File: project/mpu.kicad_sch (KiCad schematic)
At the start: 0 parts

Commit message: Added CubeMX project and some schematic components are added
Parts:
- added C1, C2: 2u2, bozi:GRM03_T09, symbol Device:C
- added C10, C11: 6p, bozi:GCM15_T05, symbol Device:C
- added C103, C105, C4, C7: 100n, bozi:GRM15_T05, symbol Device:C
- added C104, C3, C5, C6: 1u, bozi:GRM03_T09, symbol Device:C
- added C8, C9: 10p, bozi:GRM15_T05, symbol Device:C
- added R1: 240, bozi:RESC1005X37N_edit, symbol Device:R
- added R2: 0, bozi:RESC1005X37N_edit, symbol Device:R
- added R20, R21, R22: 2K4, bozi:RESC1005X37N_edit, symbol Device:R
- added R23: 3K, bozi:RESC1005X37N_edit, symbol Device:R
- added TP13, TP16, TP17, TP18, TP19: TestPoint, TestPoint:TestPoint_Pad_D1.0mm, symbol Connector:TestPoint
- added U1: ~, symbol bozi:STM32MP135FAF
- added Y1: 24MHz, bozi:ABM11AIG16000MHZ81ZT_edit, symbol Device:Crystal_GND24
- added Y2: Crystal, bozi:ABS07AIG_edit, symbol Device:Crystal
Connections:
- new net: C11.1, R2.1, Y2.1
- new net: R23.1, U1.W12 (USB_RREF)
- new net: C2.2, U1.V14 (VDDA1V1_REG)
- new net: C1.2, U1.W15 (VDDA1V8_REG)
- new net: TP13.1, U1.W3 (PWR_CPU_ON)
- new net: R1.2, U1.R20 (DDR_ZQ)
- new net BOOT0: U1.Y17 (PI4-BOOT0)
- new net BOOT1: U1.AA15 (PI5-BOOT1)
- new net BOOT2: U1.Y15 (PI6-BOOT2)
- new net DDR_A0: U1.H20 (DDR_A0)
- new net DDR_A1: U1.N21 (DDR_A1)
- new net DDR_A10: U1.L18 (DDR_A10)
- new net DDR_A11: U1.N17 (DDR_A11)
- new net DDR_A12: U1.M19 (DDR_A12)
- new net DDR_A13: U1.G19 (DDR_A13)
- new net DDR_A2: U1.G20 (DDR_A2)
- new net DDR_A3: U1.H19 (DDR_A3)
- new net DDR_A4: U1.R19 (DDR_A4)
- new net DDR_A5: U1.F20 (DDR_A5)
- new net DDR_A6: U1.R21 (DDR_A6)
- new net DDR_A7: U1.J17 (DDR_A7)
- new net DDR_A8: U1.P19 (DDR_A8)
- new net DDR_A9: U1.G21 (DDR_A9)
- new net DDR_BA0: U1.J19 (DDR_BA0)
- new net DDR_BA1: U1.P20 (DDR_BA1)
- new net DDR_BA2: U1.H18 (DDR_BA2)
- new net DDR_CKE: U1.N20 (DDR_CKE)
- new net DDR_CLKN: U1.L20 (DDR_CLKN)
- new net DDR_CLKP: U1.M20 (DDR_CLKP)
- new net DDR_DQ0: U1.B21 (DDR_DQ0)
- new net DDR_DQ1: U1.B20 (DDR_DQ1)
- new net DDR_DQ10: U1.T19 (DDR_DQ10)
- new net DDR_DQ11: U1.W20 (DDR_DQ11)
- new net DDR_DQ12: U1.W19 (DDR_DQ12)
- new net DDR_DQ13: U1.U19 (DDR_DQ13)
- new net DDR_DQ14: U1.Y21 (DDR_DQ14)
- new net DDR_DQ15: U1.Y20 (DDR_DQ15)
- new net DDR_DQ2: U1.D19 (DDR_DQ2)
- new net DDR_DQ3: U1.E19 (DDR_DQ3)
- new net DDR_DQ4: U1.B19 (DDR_DQ4)
- new net DDR_DQ5: U1.D20 (DDR_DQ5)
- new net DDR_DQ6: U1.E20 (DDR_DQ6)
- new net DDR_DQ7: U1.F19 (DDR_DQ7)
- new net DDR_DQ8: U1.T20 (DDR_DQ8)
- new net DDR_DQ9: U1.U20 (DDR_DQ9)
- new net DDR_DQM0: U1.D21 (DDR_DQM0)
- new net DDR_DQM1: U1.W21 (DDR_DQM1)
- new net DDR_DQS0N: U1.C21 (DDR_DQS0N)
- new net DDR_DQS0P: U1.C20 (DDR_DQS0P)
- new net DDR_DQS1N: U1.V21 (DDR_DQS1N)
- new net DDR_DQS1P: U1.V20 (DDR_DQS1P)
- new net DDR_ODT: U1.J21 (DDR_ODT)
- new net DIP_0: U1.AA10 (PC2)
- new net GNDREF: C1.1, C10.1, C103.2, C104.2, C105.2, C11.2, C2.1, C3.1, C4.1, C5.2, C6.2, C7.2, C8.1, C9.1, R1.1, R23.2, U1.A1 (VSS), U1.A21 (VSS), U1.AA1 (VSS), U1.AA18 (VSS_PLL2), U1.AA21 (VSS), U1.B12 (VSS), U1.D16 (VSS), U1.E11 (VSS), U1.E16 (VSS), U1.E5 (VSS), U1.E6 (VSS), U1.F17 (VSS), U1.F18 (VSS), U1.F21 (VSS), U1.F5 (VSS), U1.G12 (VSS), U1.G14 (VSS), U1.G8 (VSS), U1.H15 (VSS), U1.H7 (VSS), U1.J10 (VSS), U1.J12 (VSS), U1.K1 (VSS_PLL), U1.K10 (VSS), U1.K11 (VSS), U1.K12 (VSS), U1.K13 (VSS), U1.K21 (VSS), U1.K9 (VSS), U1.L10 (VSS), U1.L12 (VSS), U1.L15 (VSS), U1.L17 (VSS), U1.L5 (VSS), U1.M1 (VSS), U1.M10 (VSS), U1.M11 (VSS), U1.M12 (VSS), U1.M13 (VSS), U1.M7 (VSS), U1.M9 (VSS), U1.N11 (VSS), U1.P15 (VSS), U1.P7 (VSS), U1.R11 (VSS), U1.R14 (VSS), U1.R8 (VSS), U1.T1 (VSS), U1.T17 (VSS), U1.T21 (VSS), U1.T5 (VSS), U1.U11 (VSS), U1.U13 (VSS), U1.U16 (VSS), U1.U3 (VSS_ANA), U1.U5 (VSS), U1.U6 (VSS), U1.U9 (VSSA), U1.V16 (VSS), U1.V8 (VREF-), U1.W16 (VSS), U1.W17 (BYPASS_REG1V8), U1.Y14 (VSS_USBHS), Y1.2, Y1.4
- new net I2C3_SCL: R21.2, U1.D1 (PB8)
- new net I2C3_SDA: R22.1, U1.C4 (PD14)
- new net IN_24M: C9.2, U1.T3 (PH0-OSC_IN), Y1.1
- new net IN_32K67: C10.2, U1.M2 (PC14-OSC32_IN), Y2.2
- new net LCD_D/~{C}: U1.H3 (PF10)
- new net LTDC_B2: U1.C14 (PB3)
- new net LTDC_B3: U1.D8 (PE7)
- new net LTDC_B4: U1.B8 (PH14)
- new net LTDC_B5: U1.B6 (PE0)
- new net LTDC_B6: U1.B13 (PB5)
- new net LTDC_B7: U1.A9 (PE15)
- new net LTDC_CLK: TP18.1, U1.B15 (PB15)
- new net LTDC_DE: TP19.1, U1.A15 (PB9)
- new net LTDC_G2: U1.A12 (PH13)
- new net LTDC_G3: U1.A13 (PF3)
- new net LTDC_G4: U1.C8 (PD5)
- new net LTDC_G5: U1.A7 (PG0)
- new net LTDC_G6: U1.C13 (PC7)
- new net LTDC_G7: U1.B4 (PA15)
- new net LTDC_HSYNC: TP16.1, U1.B14 (PC6)
- new net LTDC_PWM: U1.B1 (PD0)
- new net LTDC_R2: U1.A10 (PG7)
- new net LTDC_R3: U1.C11 (PB12)
- new net LTDC_R4: U1.B17 (PE3)
- new net LTDC_R5: U1.B2 (PE11)
- new net LTDC_R6: U1.A2 (PA9)
- new net LTDC_R7: U1.B7 (PE9)
- new net LTDC_VSYNC: TP17.1, U1.A4 (PE12)
- new net NRST: C105.1, U1.Y11 (NRST)
- new net OUT_24M: C8.2, U1.U2 (PH1-OSC_OUT), Y1.3
- new net OUT_32K67: R2.2, U1.L3 (PC15-OSC32_OUT)
- new net PMIC_WAKEUP: U1.M3 (PC13)
- new net PWR_ON: U1.U17 (PWR_ON)
- new net SDMMC1_CK: U1.A19 (PC12)
- new net SDMMC1_CMD: U1.C19 (PD2)
- new net SDMMC1_D0: U1.C18 (PC8)
- new net SDMMC1_D1: U1.A20 (PC9)
- new net SDMMC1_D2: U1.A18 (PC10)
- new net SDMMC1_D3: U1.B18 (PC11)
- new net SDMMC1_DETECT: U1.A16 (PF0)
- new net SPI1_MISO: U1.U10 (PA6)
- new net SPI1_MOSI: U1.W5 (PC0)
- new net SPI1_NSS: U1.Y5 (PA5)
- new net SPI1_SCK: U1.V6 (PA7)
- new net SPI5_MISO: U1.H2 (PE4)
- new net SPI5_MOSI: U1.D3 (PH12)
- new net SPI5_NSS: R20.2, U1.G1 (PF6)
- new net SPI5_SCK: U1.G2 (PG10)
- new net T_JCLK/T_SWCLK: U1.Y2 (PF14)
- new net T_JTDI: U1.Y19 (PH4)
- new net T_JTDO/T_SWO: U1.W18 (PH5)
- new net T_JTMS/T_SWDIO: U1.Y12 (PF15)
- new net UART4_RX: U1.B5 (PD8)
- new net UART4_TX: U1.D2 (PD6)
- new net UART5_CTS: U1.W6 (PC3)
- new net UART5_RTS: U1.Y7 (PC4)
- new net UART5_RX: U1.W4 (PF13)
- new net UART5_TX: U1.Y3 (PA0)
- new net USART6_RX: U1.F2 (PG9)
- new net USART6_TX: U1.F1 (PF8)
- new net USB_D1_N: U1.AA16 (USB_DM1)
- new net USB_D1_P: U1.Y16 (USB_DP1)
- new net USB_PWR_CC1: U1.AA4 (PF12)
- new net USB_PWR_CC2: U1.W9 (PA3)
- new net USR_LD1: U1.Y10 (PG14)
- new net USR_LD2: U1.Y9 (PC1)
- new net USR_LD3: U1.Y8 (PB1)
- new net VDD: C5.1, C6.1, R20.1, R21.1, R22.2, U1.AA12 (PDR_ON), U1.C15 (VDDSD2), U1.E12 (VDD), U1.E17 (VDDSD1), U1.G13 (VDD), U1.G9 (VDD), U1.J13 (VDD), U1.J7 (VDD), U1.J9 (VDD), U1.K2 (VDD_PLL), U1.L2 (VBAT), U1.M5 (VDD), U1.N12 (VDD), U1.N7 (VDD), U1.N9 (VDD), U1.R12 (VDD), U1.R5 (VDD), U1.R7 (VDD), U1.R9 (VDD), U1.U7 (VDD), U1.V2 (VDD_ANA), U1.W11 (VDD), U1.Y18 (VDD_PLL2)
- new net VDD_ADC: C103.1, C104.1, C3.2, U1.U8 (VDDA), U1.W7 (VREF+)
- new net VDD_CORE: U1.G11 (VDDCORE), U1.J11 (VDDCORE), U1.J15 (VDDCORE), U1.L13 (VDDCORE), U1.L7 (VDDCORE), U1.L9 (VDDCORE), U1.N10 (VDDCORE), U1.N13 (VDDCORE), U1.N15 (VDDCORE), U1.R10 (VDDCORE), U1.R13 (VDDCORE), U1.U12 (VDDCORE), U1.U14 (VDDCORE)
- new net VDD_CPU: U1.E10 (VDDCPU), U1.E7 (VDDCPU), U1.G10 (VDDCPU), U1.G5 (VDDCPU), U1.G7 (VDDCPU), U1.K5 (VDDCPU), U1.K7 (VDDCPU)
- new net VDD_DDR: U1.E15 (VDDQ_DDR), U1.G15 (VDDQ_DDR), U1.G17 (VDDQ_DDR), U1.K15 (VDDQ_DDR), U1.K17 (VDDQ_DDR), U1.M15 (VDDQ_DDR), U1.M17 (VDDQ_DDR), U1.R15 (VDDQ_DDR), U1.R17 (VDDQ_DDR), U1.U15 (VDDQ_DDR)
- new net VDD_USB: C4.2, U1.W14 (VDD3V3_USBHS)
- new net VREF_DDR: C7.1, U1.T18 (DDR_VREF)
- new net ~{DDR_CAS}: U1.L19 (DDR_CASN)
- new net ~{DDR_CS}: U1.J20 (DDR_CSN)
- new net ~{DDR_RAS}: U1.K20 (DDR_RASN)
- new net ~{DDR_RESET}: U1.H17 (DDR_RESETN)
- new net ~{DDR_WE}: U1.K19 (DDR_WEN)
- no-connect marks 0 -> 76
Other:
- note added: "LOWER"
- note added: "UPPER"

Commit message: schemtic is done, need to go through BOM
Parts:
- removed R20: 2K4, bozi:RESC1005X37N_edit, symbol Device:R
- removed TP16, TP17, TP18, TP19: TestPoint, TestPoint:TestPoint_Pad_D1.0mm, symbol Connector:TestPoint
- added R62, R63: 2.4K, bozi:RESC1005X37N_edit, symbol Device:R
- C1, C2: value 2u2 -> 2.2uF; Manufacturer_Name (none) -> Murata Electronics
- C10: renamed from C105; value 100n -> 100nF; Manufacturer_Name (none) -> Murata Electronics
- C11: renamed from C8; value 10p -> 10pF; Manufacturer_Name (none) -> Murata Electronics
- C12: renamed from C9; value 10p -> 10pF; Manufacturer_Name (none) -> Murata Electronics
- C13: renamed from C10; value 6p -> 6pF; Manufacturer_Name (none) -> Murata Electronics
- C14: renamed from C11; value 6p -> 6pF; Manufacturer_Name (none) -> Murata Electronics
- C3, C5, C6: value 1u -> 1uF; Manufacturer_Name (none) -> Murata Electronics
- C4: value 100n -> 100nF; Manufacturer_Name (none) -> Murata Electronics
- C7: renamed from C103; value 100n -> 100nF; Manufacturer_Name (none) -> Murata Electronics
- C8: renamed from C104; value 1u -> 1uF; Manufacturer_Name (none) -> Murata Electronics
- C9: renamed from C7; value 100n -> 100nF; Manufacturer_Name (none) -> Murata Electronics
- R1: renamed from R21; value 2K4 -> 2.4K; Manufacturer_Name (none) -> YAGEO
- R3: renamed from R22; value 2K4 -> 2.4K; Manufacturer_Name (none) -> YAGEO
- R4: renamed from R23; Manufacturer_Name (none) -> YAGEO
- R5: renamed from R1; value 240 -> 240R; Manufacturer_Name (none) -> YAGEO
- R6: renamed from R2; value 0 -> 0R; Manufacturer_Name (none) -> YAGEO; Manufacturer_Part_Number AA0402JR-070RL -> RC0402JR-070RL
- U1: value ~ -> STM32MP135F; footprint (none) -> bozi:BGA320C50P21X21_1100X1100X120_edit; Manufacturer_Name (none) -> STMicroelectronics; Manufacturer_Part_Number (none) -> STM32MP135FAF7
- Y1: value 24MHz -> Crystal 24 MHz; Manufacturer_Name (none) -> Abracon LLC
- Y2: value Crystal -> Crystal 32.67 KHz; Manufacturer_Name (none) -> Abracon LLC
- renumbered TP13 to TP5
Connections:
- net SPI5_MOSI is gone; now on net I2C3_SCL: U1.D3 (PH12)
- net I2C3_SCL: no longer U1.D1 (PB8)
- net I2C3_SDA: now also U1.E3 (PH8); no longer U1.C4 (PD14)
- net VDD: now also R62.2, R63.2
- net WIFI_BLE_GPIO0: now reaches U1.AA2 (PB11)
- net USART2_RTS: now reaches U1.AA3 (PA1)
- net USART2_CTS: now reaches U1.AA7 (PC5)
- net FMC_NE3: now reaches U1.C1 (PB6)
- net FMC_D3: now reaches U1.C5 (PD1)
- net FMC_NOE: now reaches U1.C7 (PD4)
- net FMC_D1: now reaches U1.E9 (PD15)
- net SAI1_CK1: now reaches U1.J2 (PD13)
- net SAI1_D1: now reaches U1.J3 (PB2)
- net I2C4_SDA: now reaches U1.P2 (PA8)
- net I2C4_SDA: now also R62.1
- net USART2_TX: now reaches U1.Y4 (PA2)
- net USB_PWR_GPIO0: now reaches U1.A3 (PE13)
- net FMC_D5: now reaches U1.B9 (PE8)
- net FMC_D7: now reaches U1.C10 (PE10)
- net SAI2_SD_A: now reaches U1.C17 (PG6)
- net SAI2_FS_B: now reaches U1.J1 (PH7)
- net I2C4_SCL: now reaches U1.N1 (PE2)
- net I2C4_SCL: now also R63.1
- net IO_EX_GPIO0: now reaches U1.R2 (PG11)
- net SAI2_SCK_B: now reaches U1.T2 (PE6)
- net SAI2_SD_B: now reaches U1.W1 (PG3)
- net DIP_0: no longer names the net of U1.AA10 (PC2)
- net LCD_D/~{C}: no longer names the net of U1.H3 (PF10)
- net LTDC_B2: no longer names the net of U1.C14 (PB3)
- net LTDC_B3 renamed FMC_D4
- net LTDC_B4: no longer names the net of U1.B8 (PH14)
- net LTDC_B5: no longer names the net of U1.B6 (PE0)
- net LTDC_B6: no longer names the net of U1.B13 (PB5)
- net LTDC_B7: no longer names the net of U1.A9 (PE15)
- net LTDC_CLK: no longer names the net of U1.B15 (PB15)
- net LTDC_DE renamed DISPLAY_GPIO0
- net LTDC_G2: no longer names the net of U1.A12 (PH13)
- net LTDC_G3 renamed FMC_A3
- net LTDC_G4 renamed FMC_NWE
- net LTDC_G5: no longer names the net of U1.A7 (PG0)
- net LTDC_G6: no longer names the net of U1.C13 (PC7)
- net LTDC_G7: no longer names the net of U1.B4 (PA15)
- net LTDC_HSYNC renamed DISPLAY_GPIO1
- net LTDC_PWM renamed FMC_D2
- net LTDC_R2: no longer names the net of U1.A10 (PG7)
- net LTDC_R3: no longer names the net of U1.C11 (PB12)
- net LTDC_R4: no longer names the net of U1.B17 (PE3)
- net LTDC_R5 renamed BFG_GPIO0
- net LTDC_R6 renamed VSOURCE_GPIO0
- net LTDC_R7 renamed FMC_D6
- net LTDC_VSYNC renamed USB_PWR_GPIO1
- net PMIC_WAKEUP: no longer names the net of U1.M3 (PC13)
- net SPI5_MISO: no longer names the net of U1.H2 (PE4)
- net SPI5_NSS renamed PMIC_GPIO1
- net SPI5_SCK: no longer names the net of U1.G2 (PG10)
- net UART5_CTS: no longer names the net of U1.W6 (PC3)
- net UART5_RTS: no longer names the net of U1.Y7 (PC4)
- net USART6_RX: no longer names the net of U1.F2 (PG9)
- net USART6_TX renamed PMIC_GPIO0
- net USB_PWR_CC1: no longer names the net of U1.AA4 (PF12)
- net USB_PWR_CC2 renamed USART2_RX
- net USR_LD1: no longer names the net of U1.Y10 (PG14)
- net USR_LD2: no longer names the net of U1.Y9 (PC1)
- net USR_LD3: no longer names the net of U1.Y8 (PB1)
- new net FMC_D0: U1.C4 (PD14)
- no-connect marks 76 -> 81
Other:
- moved on the sheet: U1C

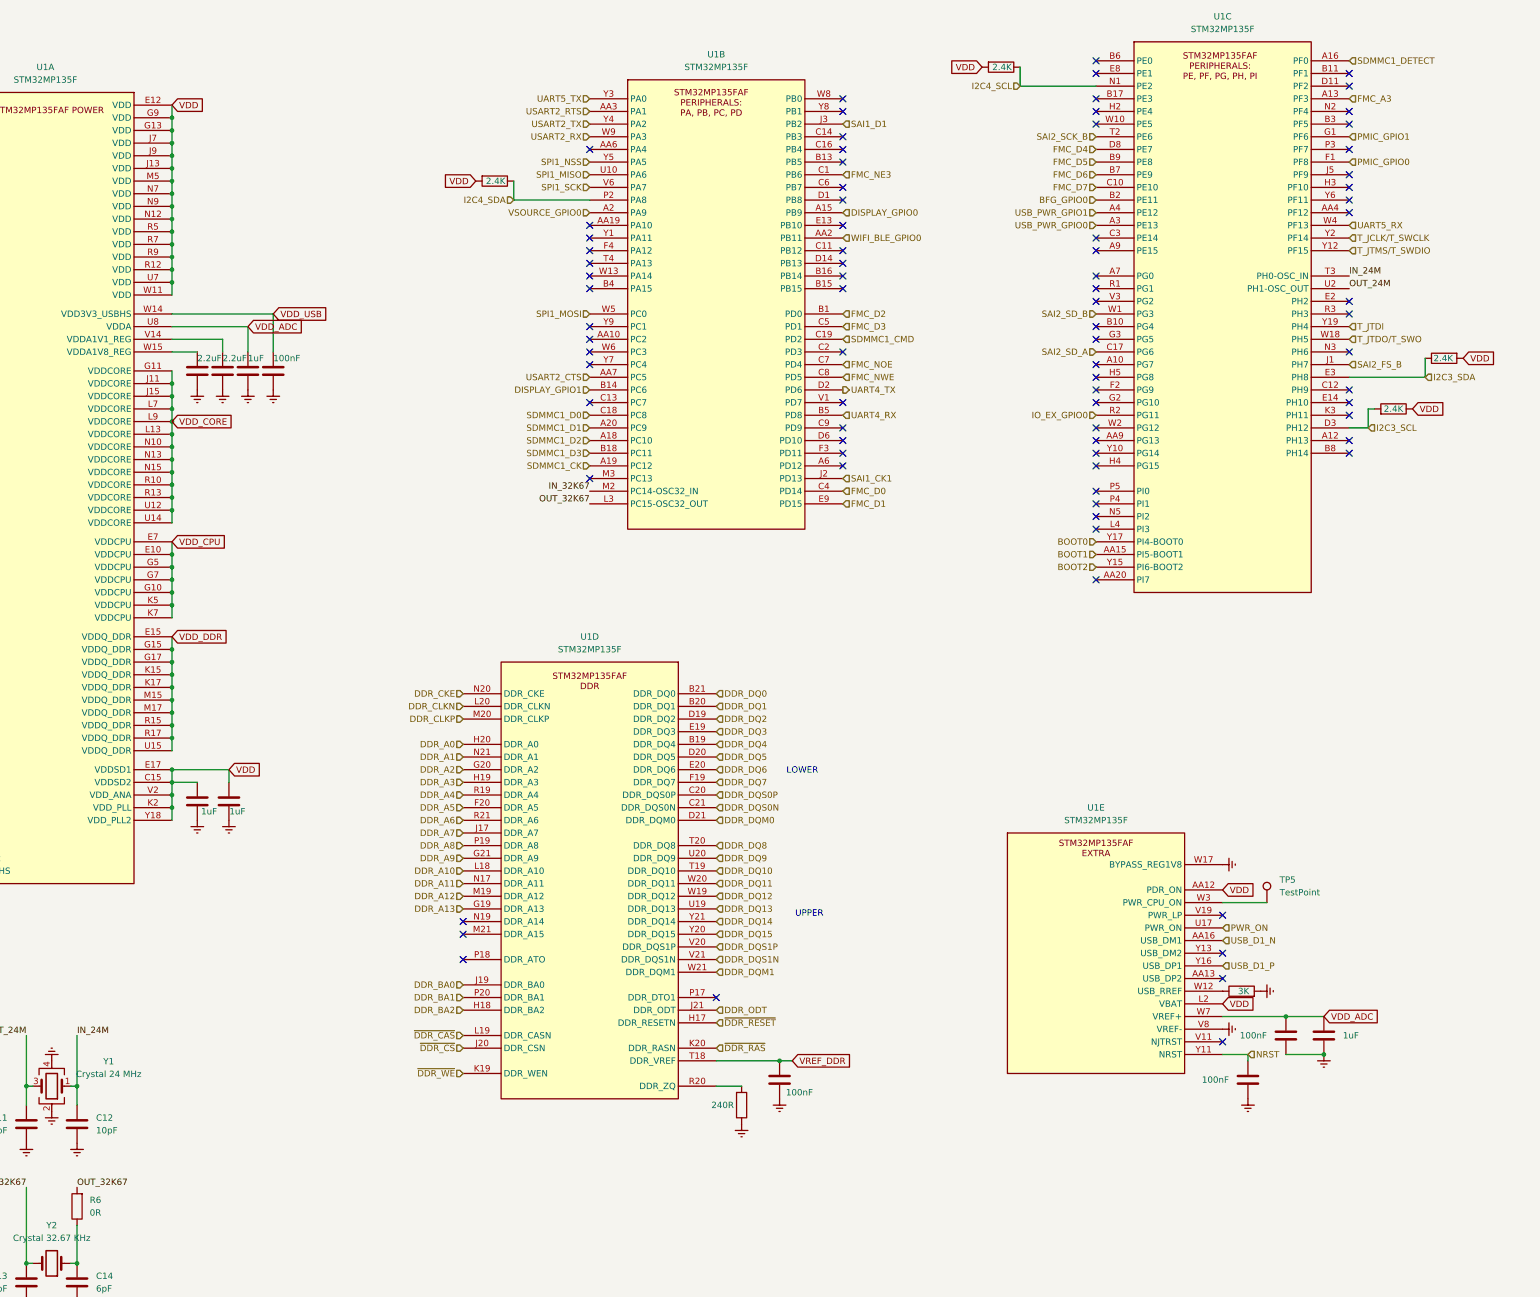
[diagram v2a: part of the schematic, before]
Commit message: schemtic is done, annotation set
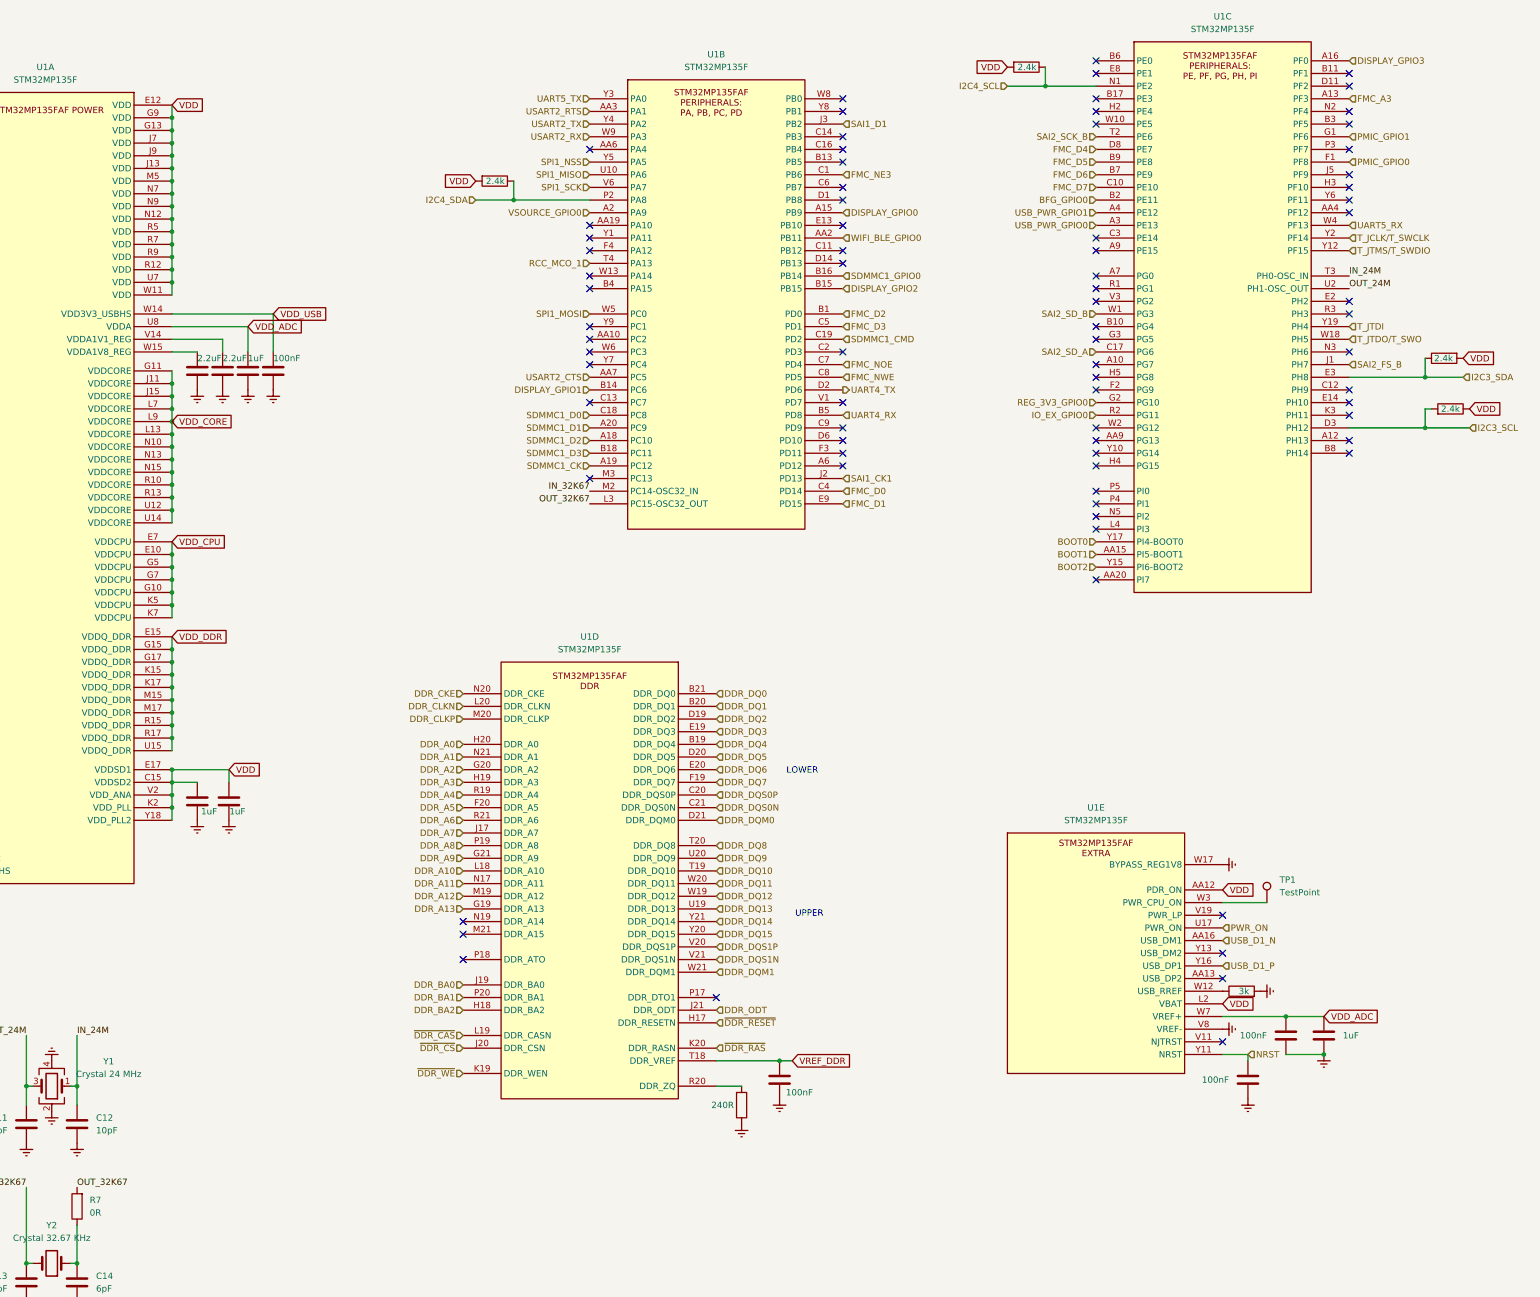
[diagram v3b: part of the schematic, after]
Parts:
- R1: renamed from R63; value 2.4K -> 2.4k
- R2: renamed from R62; value 2.4K -> 2.4k
- R3: value 2.4K -> 2.4k
- R4: renamed from R1; value 2.4K -> 2.4k
- R5: renamed from R4; value 3K -> 3k
- renumbered R5 to R6, R6 to R7, TP5 to TP1
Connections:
- net DISPLAY_GPIO2: now reaches U1.B15 (PB15)
- net SDMMC1_GPIO0: now reaches U1.B16 (PB14)
- net RCC_MCO_1: now reaches U1.T4 (PA13)
- net REG_3V3_GPIO0: now reaches U1.G2 (PG10)
- net SDMMC1_DETECT renamed DISPLAY_GPIO3
- no-connect marks 81 -> 77
